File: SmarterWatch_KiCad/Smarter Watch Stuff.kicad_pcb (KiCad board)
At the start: 4 copper layers, 39.5 x 39.5 mm, 73 parts, among them J3 CX70M-24P1, M1 Motor_DC, Q1 2N7002, Q2 2N7002, Q3 2N7002, Q4 2N7002, SW1 SW_SPST, SW2 SW_SPST, U1 MCP7940N-xSN, U10 MAX30102, U11 BMI160, U12 M24C64-WMN6TP, U2 TSL25911FN, U3 MCP73831-2-MC, U4 TCR2EE10, U5 ESP32-C6-MINI-1, U6 SHTC3, U7 TMP117xxDRV, U9 MIC5365-1.8YC5, Y1 Crystal

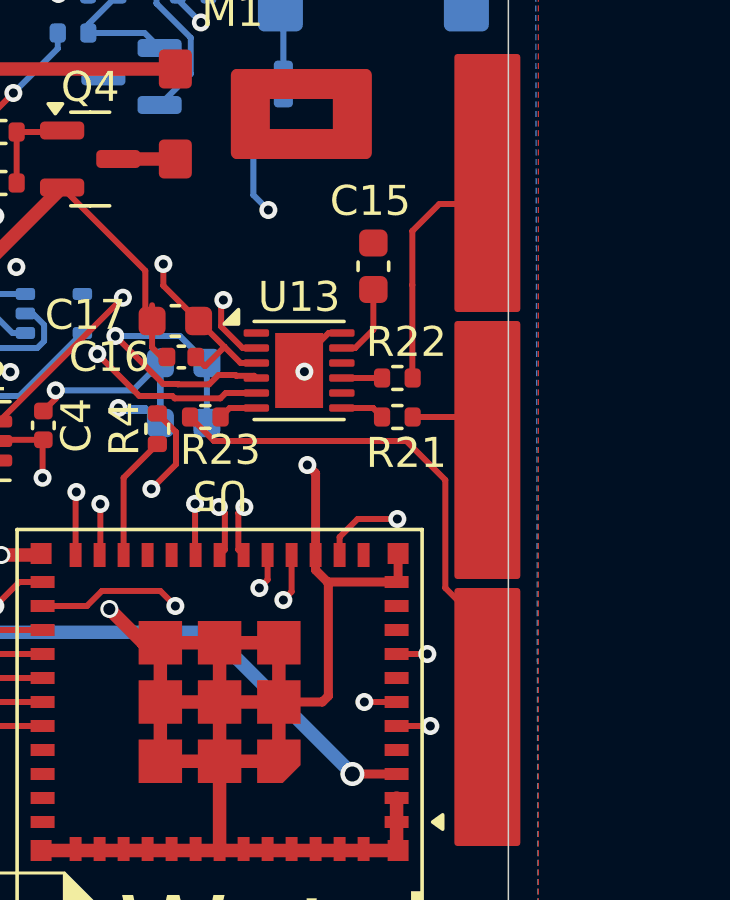
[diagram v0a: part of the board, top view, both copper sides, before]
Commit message: Fixed problem with CapSense
Added traces to ensure pad connection
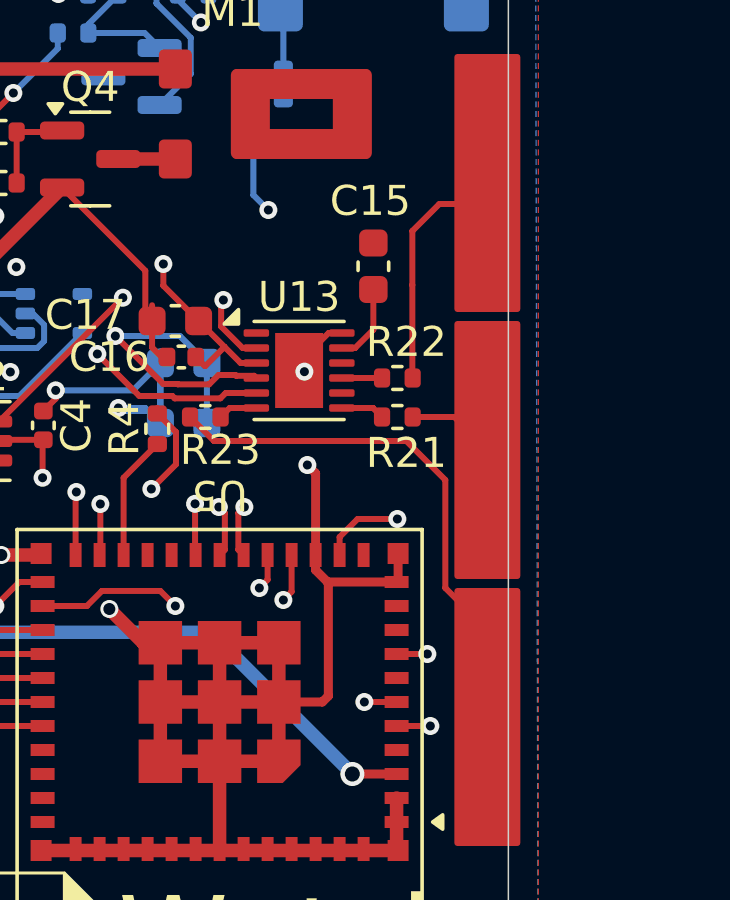
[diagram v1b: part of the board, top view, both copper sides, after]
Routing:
- net CRX2: track 13.8 -> 17.9 mm
- net CRX0: track 2.49 -> 4.35 mm
- net CRX1: track 7.48 -> 9.27 mm
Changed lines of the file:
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@@
 	(segment
 		(start 68.81 79.1)
+		(end 69.9 79.1)
+		(width 0.2)
+		(layer "F.Cu")
+		(net 92)
+	)
+	(segment
+		(start 69.9 79.1)
 		(end 71.3 79.1)
+		(width 0.2)
+		(layer "F.Cu")
+		(net 92)
+	)
+	(segment
+		(start 69.9 79.1)
+		(end 70.2 79.1)
+		(width 0.2)
+		(layer "F.Cu")
+		(net 92)
+	)
+	(segment
+		(start 70.2 79.1)
+		(end 71.3 80.2)
 		(width 0.2)
 		(layer "F.Cu")
@@
 	)
 	(segment
+		(start 69.8 72)
+		(end 71 72)
+		(width 0.2)
+		(layer "F.Cu")
+		(net 94)
+	)
+	(segment
 		(start 68.8 72.9)
 		(end 69.7 72)
@@
 	(segment
 		(start 69.7 72)
-		(end 71 72)
+		(end 69.8 72)
 		(width 0.2)
 		(layer "F.Cu")
@@
 		(start 68.8 77.79)
 		(end 68.8 74.7)
+		(width 0.2)
+		(layer "F.Cu")
+		(net 94)
+	)
+	(segment
+		(start 70.6 72)
+		(end 71.3 71.3)
+		(width 0.2)
+		(layer "F.Cu")
+		(net 94)
+	)
+	(segment
+		(start 69.8 72)
+		(end 70.6 72)
 		(width 0.2)
 		(layer "F.Cu")
@@
 	(segment
 		(start 69.899 84.799)
-		(end 69.899 81.199)
+		(end 71.3 86.2)
 		(width 0.2)
 		(layer "F.Cu")
@@
 	)
 	(segment
-		(start 70.5 85.4)
-		(end 69.899 84.799)
+		(start 69.899 84.799)
+		(end 69.899 81.199)
 		(width 0.2)
 		(layer "F.Cu")
@@
 		(width 0.2)
 		(layer "F.Cu")
+		(net 95)
+	)
+	(segment
+		(start 71.3 86.2)
+		(end 71.3 89.1)
+		(width 0.2)
+		(layer "F.Cu")

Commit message: checking sum schematic and touching the wires together forever
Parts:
- added R24: 33k, Resistor_SMD:R_0402_1005Metric, F.Cu at (39.8, 87.3)
- added R25: 33k, Resistor_SMD:R_0402_1005Metric, F.Cu at (34.8, 87.3)
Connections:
- J3 pad A5: unconnected-(J3-PadA5) -> Net-(J3-PadA5)
- J3 pad B5: unconnected-(J3-PadB5) -> Net-(J3-PadB5)
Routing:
- net Screen_power: track 24.6 -> 47.7 mm
- net Net-(J3-PadA5): track 0.00 -> 11.7 mm, vias 0 -> 3
- net Net-(J3-PadB5): track 0.00 -> 9.26 mm, vias 0 -> 2
- net +5V: track 26.6 -> 31.4 mm, vias 2 -> 3
- net USB_D+: track 27.2 -> 31.6 mm
- net USB_D-: track 28.0 -> 29.3 mm
- net GND: track 233.9 -> 234.4 mm

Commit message: more syncing
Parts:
- removed R24, R25: 33k, Resistor_SMD:R_0402_1005Metric
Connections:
- J3 pad A5: Net-(J3-PadA5) -> unconnected-(J3-PadA5)
- J3 pad B5: Net-(J3-PadB5) -> unconnected-(J3-PadB5)
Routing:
- net Screen_power: track 47.7 -> 24.6 mm
- net Net-(J3-PadA5): track 11.7 -> 0.00 mm, vias 3 -> 0
- net Net-(J3-PadB5): track 9.26 -> 0.00 mm, vias 2 -> 0
- net +5V: track 31.4 -> 26.6 mm, vias 3 -> 2
- net USB_D+: track 31.6 -> 27.2 mm
- net USB_D-: track 29.3 -> 28.0 mm
- net GND: track 234.4 -> 233.9 mm

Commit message: Sync
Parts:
- removed G***: LOGO, Smarter watching stuff foot:SW_logo
- added R24: 33k, Resistor_SMD:R_0402_1005Metric, F.Cu at (163.6, 128.1)
- added R25: 33k, Resistor_SMD:R_0402_1005Metric, F.Cu at (163.6, 130.0)
- C1, C10, C11, C12, C13, C18, C19, C2, C3, C6, C9, J1, J2, J4, J5, J6, Q2, Q3, R12, R13, R14, R15, R3, R5, SW1, SW2, U1, U10, U9, Y1: moved to F.Cu
- moved U4 155.2 mm to (165.3, 157.5)
- moved C7 154.9 mm to (165.0, 160.0), turned to 0 degrees
- moved C1 150.2 mm to (160.2, 156.8), turned to 0 degrees
- moved D2 145.8 mm to (141.4, 164.8)
- moved C6 143.9 mm to (145.8, 158.1), turned to 0 degrees
- moved C3 142.2 mm to (160.2, 160.8)
- moved U1 142.0 mm to (154.5, 159.2), turned to 0 degrees
- moved R18 141.0 mm to (160.2, 152.2), turned to 0 degrees
- moved Y1 140.0 mm to (152.9, 164.2), turned to 0 degrees
- moved C2 139.3 mm to (160.2, 158.8)
- moved R17 137.9 mm to (160.2, 150.2), turned to 0 degrees
- moved C5 137.8 mm to (145.8, 156.1), turned to 0 degrees
- moved R2 137.8 mm to (142.9, 158.1)
- moved J6 136.3 mm to (159.1, 144.5), turned to 0 degrees
- moved R16 134.7 mm to (160.2, 148.2), turned to 0 degrees
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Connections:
- J3 pad A5: unconnected-(J3-PadA5) -> Net-(J3-PadA5)
- J3 pad B5: unconnected-(J3-PadB5) -> Net-(J3-PadB5)
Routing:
- net GND: track 233.9 -> 0.00 mm, vias 23 -> 0
- net +3.3V: track 98.8 -> 0.00 mm, vias 11 -> 0
- net SDA: track 96.6 -> 0.00 mm, vias 6 -> 0
- net SCL: track 91.4 -> 0.00 mm, vias 7 -> 0
- net +3.3V_sensor: track 66.2 -> 0.00 mm, vias 7 -> 0
- net Backlight: track 40.7 -> 0.00 mm, vias 4 -> 0
- net +BATT: track 39.0 -> 0.00 mm
- net RGB_DIN: track 37.0 -> 0.00 mm, vias 2 -> 0
- net Screen_Reset: track 34.6 -> 0.00 mm, vias 1 -> 0
- net SCLK: track 34.2 -> 0.00 mm, vias 2 -> 0
- net Screen_A0: track 34.0 -> 0.00 mm, vias 1 -> 0
- net MOSI: track 31.4 -> 0.00 mm, vias 2 -> 0
- net Net-(SW1-B): track 31.1 -> 0.00 mm, vias 2 -> 0
- net USB_D-: track 28.0 -> 0.00 mm, vias 2 -> 0
- net Screen_CS: track 27.9 -> 0.00 mm, vias 1 -> 0
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- removed copper zone on B.Cu, net +3.3V
- removed copper zone on F.Cu, net GND
- removed copper zone on In1.Cu, net GND
- removed copper zone on In2.Cu, net GND
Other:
- board outline removed
- board text removed: "BOOT"
- board text removed: "Made by Julian Halloran and Ahmad Baig"
- board text removed: "RESET"
- board text removed: "Smarter"
- board text removed: "SmarterWatch V1.0 A Watch with a lot of useless features Designed by Julian and Ahmad"
- board text removed: "Watch"

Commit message: backups and freidnds
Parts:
- moved U11 42.7 mm to (131.6, 132.4), turned to 45 degrees
- moved J4 40.9 mm to (120.9, 118.0)
- moved J1 28.2 mm to (118.0, 118.0)
- moved J2 26.8 mm to (115.0, 118.0)
- moved U8 23.5 mm to (141.0, 125.4), turned to -90 degrees
- moved J5 21.6 mm to (134.4, 140.0)
- moved J6 21.6 mm to (138.0, 140.0)
- moved SW1 20.3 mm to (109.1, 117.0)
- moved U5 17.1 mm to (109.0, 128.1), turned to 90 degrees
